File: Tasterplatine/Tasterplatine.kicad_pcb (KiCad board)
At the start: 2 copper layers, 26.9 x 39.9 mm, 3 parts, among them J1 2,5 MSFW 06, SW1 Marquardt 1010.8502

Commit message: pins
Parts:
- moved J1 12.5 mm to (53.2, 78.5), turned to 0 degrees
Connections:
- J1 pad 1: Net-(J1-Pin_1) -> /FREI
- J1 pad 2: Net-(J1-Pin_2) -> /LS
- J1 pad 3: Net-(J1-Pin_3) -> /LZ
- J1 pad 4: Net-(J1-Pin_4) -> /+12V
- J1 pad 5: Net-(J1-Pin_5) -> /ZE5
- J1 pad 6: unconnected-(J1-Pin_6-Pad6) -> /TASTE
- LA1 pad 1: Net-(J1-Pin_5) -> /LS
- LA1 pad 2: Net-(J1-Pin_4) -> /LZ
- SW1 pad 1: Net-(J1-Pin_2) -> /ZE5
- SW1 pad 2: Net-(J1-Pin_3) -> /+12V
- SW1 pad 3: Net-(J1-Pin_1) -> /TASTE
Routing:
- net Net-(J1-Pin_3): track 33.7 -> 0.00 mm, vias 1 -> 0
- net /+12V: track 0.00 -> 33.1 mm, vias 0 -> 1
- net Net-(J1-Pin_2): track 24.7 -> 0.00 mm
- net /ZE5: track 0.00 -> 24.7 mm
- net Net-(J1-Pin_1): track 22.8 -> 0.00 mm
- net /TASTE: track 0.00 -> 22.8 mm
- net Net-(J1-Pin_5): track 19.3 -> 0.00 mm
- net /LS: track 0.00 -> 19.3 mm
- net Net-(J1-Pin_4): track 18.9 -> 0.00 mm
- net /LZ: track 0.00 -> 18.9 mm
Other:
- board size 26.9 x 39.9 mm -> 27.4 x 40 mm

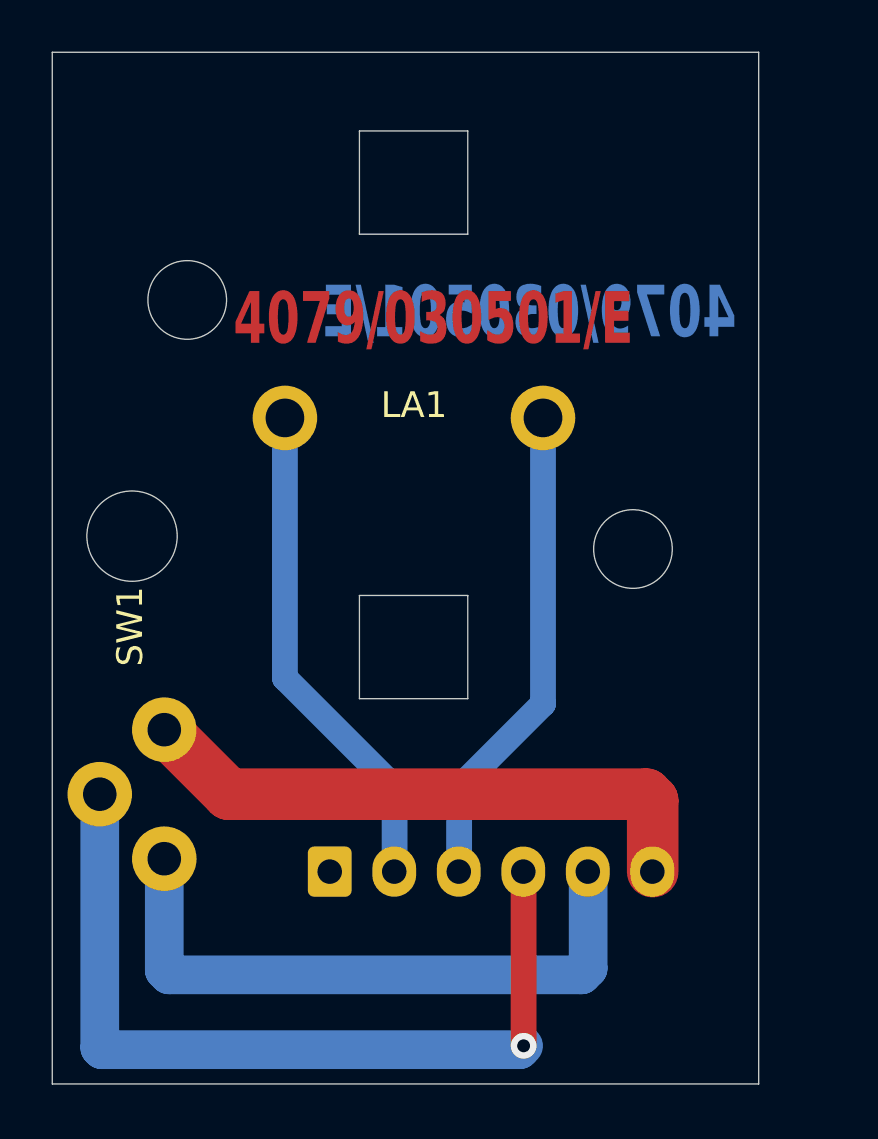
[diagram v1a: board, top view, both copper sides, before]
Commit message: taster LED
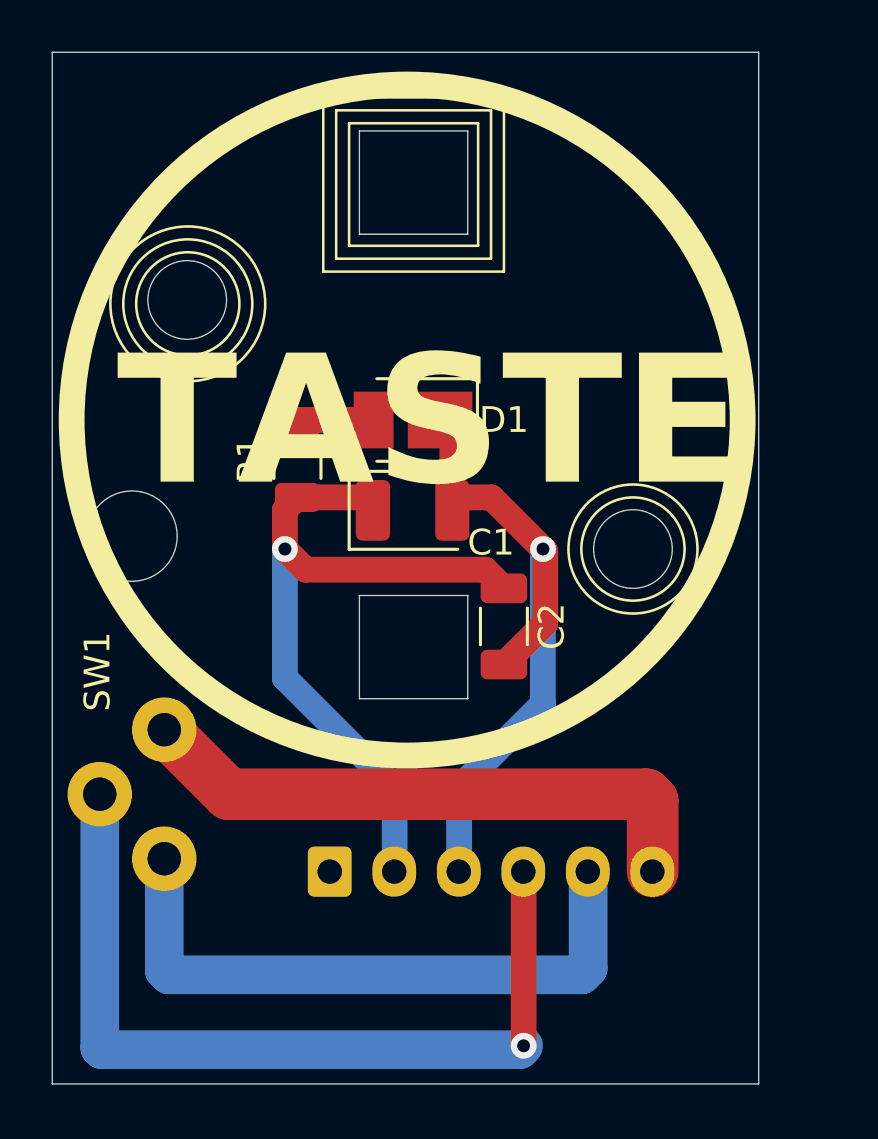
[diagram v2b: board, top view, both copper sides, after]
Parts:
- removed LA1: T10 10x27 W2,1x9,5d 6V 2W, Taster:LampSocket
- added C1: 47uF, Capacitor_Tantalum_SMD:CP_EIA-3528-12_Kemet-T, F.Cu at (56.5, 64.5)
- added C2: 1uF, Capacitor_SMD:C_1206_3216Metric, F.Cu at (60.0, 69.0)
- added D1: LED, LED_SMD:LED_PLCC_2835_Handsoldering, F.Cu at (56.5, 61.0)
- added R1: 100, Resistor_SMD:R_1206_3216Metric, F.Cu at (52.0, 62.5)
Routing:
- net /LS: track 19.3 -> 28.5 mm, vias 0 -> 1
- net /LZ: track 18.9 -> 26.9 mm, vias 0 -> 1
- net Net-(D1-A): track 0.00 -> 2.98 mm
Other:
- board text added: "TASTE"
- board text removed: "4079/030501/E"
